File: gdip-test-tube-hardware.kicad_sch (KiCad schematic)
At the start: 52 parts, among them J1 USB_B, J2 USB_B, J3 Conn_01x06, J4 Conn_01x06, J5 Conn_01x06, J6 Screw_Terminal_01x02, Q1 BC818, Q2 BC818, Q3 BC818, SW1 SW_Push, SW2 SW_Push, U1 ESP32-S3-WROOM-1-N16R2, U2 AMS1117-3.3, U3 CP2102N-Axx-xQFN28, U4 USBLC6-2SC6, U5 USBLC6-2SC6, U6 74LVC2G00

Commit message: Removed multiplexer for buzzer and servo as we can remap any ESP32 pin. Also switched mux for shift register for the 7-seg display.
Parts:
- removed J3, J4, J5: Conn_01x06, Connector_PinHeader_2.54mm:PinHeader_1x06_P2.54mm_Vertical, symbol Connector_Generic:Conn_01x06
- added J3: Screw_Terminal_01x02, gdip-test-tube:TE_282837-2, symbol Connector:Screw_Terminal_01x02
- added R18, R19, R20, R21, R22, R23, R24, R25: 330, Resistor_SMD:R_0805_2012Metric, symbol Device:R_Small
- added SERVO_A1, SERVO_B1, SERVO_C1, SERVO_D1, SERVO_E1, SERVO_F1: Conn_01x03_Pin, Connector:FanPinHeader_1x03_P2.54mm_Vertical, symbol Connector:Conn_01x03_Pin
- added U7: HDSP-7401, Display_7Segment:HDSP-7401, symbol Display_Character:HDSP-7401
- added U8: 74AHC595, Package_SO:SOIC-16_3.9x9.9mm_P1.27mm, symbol 74xx:74AHC595
- LS1: footprint PKLCS1212E40A1-R1:SPKR_PKLCS1212E40A1-R1 -> gdip-test-tube:SPKR_PKLCS1212E40A1-R1
- U4: JLCPCB (none) -> C2687116
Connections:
- net +3.3V: now also U7.1 (CA), U7.6 (CA), U8.10 (~{SRCLR}), U8.16 (VCC)
- net +5V: now also J3.1 (Pin_1), SERVO_A1.1 (Pin_1), SERVO_B1.1 (Pin_1), SERVO_C1.1 (Pin_1), SERVO_D1.1 (Pin_1), SERVO_E1.1 (Pin_1), SERVO_F1.1 (Pin_1); no longer J6.1 (Pin_1)
- net D1+_IN: now also U4.1 (I/O1); no longer U4.3 (I/O2)
- net D1+_OUT: now also U3.4 (D+), U4.6 (I/O1); no longer U4.4 (I/O2)
- net D1-_IN: now also U4.3 (I/O2); no longer U4.1 (I/O1)
- net D1-_OUT: now also U3.5 (D-), U4.4 (I/O2); no longer U4.6 (I/O1)
- net D2+_OUT: no longer U3.4 (D+)
- net D2-_OUT: no longer U3.5 (D-)
- net GND: now also J3.2 (Pin_2), SERVO_A1.3 (Pin_3), SERVO_B1.3 (Pin_3), SERVO_C1.3 (Pin_3), SERVO_D1.3 (Pin_3), SERVO_E1.3 (Pin_3), SERVO_F1.3 (Pin_3), U8.13 (~{OE}), U8.8 (GND); no longer J6.2 (Pin_2)
- net PWM1: now also SERVO_A1.2 (Pin_2)
- net PWM2: now also SERVO_B1.2 (Pin_2)
- net PWM3: now also SERVO_C1.2 (Pin_2)
- net PWM4: now also SERVO_D1.2 (Pin_2)
- net PWM5: now also SERVO_E1.2 (Pin_2)
- net PWM6: now reaches U6.2
- net PWM6: now also U1.17 (IO9)
- net PWMX: now reaches U1.12 (IO8)
- net PWMX: now also SERVO_F1.2 (Pin_2)
- net GPIO_SR_DATA: now reaches U1.18 (IO10)
- net GPIO_SR_DATA: now also U8.14 (SER)
- net GPIO_SR_CLOCK: now reaches U1.19 (IO11)
- net GPIO_SR_CLOCK: now also U8.11 (SRCLK)
- net GPIO_SR_RCLK: now reaches U1.20 (IO12)
- net GPIO_SR_RCLK: now also U8.12 (RCLK)
- new net: R19.1, U8.1 (QB)
- new net: R19.2, U7.9 (B)
- new net: R18.1, U8.15 (QA)
- new net: R20.1, U8.2 (QC)
- new net: R21.1, U8.3 (QD)
- new net: R25.1, U8.4 (QE)
- new net: R22.1, U8.5 (QF)
- new net: R23.1, U8.6 (QG)
- new net: R24.1, U8.7 (QH)
- new net: R20.2, U7.8 (C)
- new net: R24.2, U7.7 (DP)
- new net: R23.2, U7.3 (G)
- new net: R18.2, U7.10 (A)
- new net: R25.2, U7.4 (E)
- new net: R22.2, U7.2 (F)
- new net: R21.2, U7.5 (D)
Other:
- note added: "Mounting Holes"
- note added: "SEVEN SEGMENT"
- note added: "Warning LEDs"
- note removed: "Power Pin Headers"
- moved on the sheet: C1, C2, C4, C5, C6, C8, C9, H1, H2, H3, H4, J1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

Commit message: Further work on layout.
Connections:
- net +5V: now also SERVO_A1.2 (Pin_2), SERVO_B1.2 (Pin_2), SERVO_C1.2 (Pin_2), SERVO_D1.2 (Pin_2), SERVO_E1.2 (Pin_2), SERVO_F1.2 (Pin_2); no longer SERVO_A1.1 (Pin_1), SERVO_B1.1 (Pin_1), SERVO_C1.1 (Pin_1), SERVO_D1.1 (Pin_1), SERVO_E1.1 (Pin_1), SERVO_F1.1 (Pin_1)
- net GPIO_SR_CLOCK: now also U1.20 (IO12); no longer U1.19 (IO11)
- net GPIO_SR_RCLK: now also U1.19 (IO11); no longer U1.20 (IO12)
- net PWM1: now also SERVO_D1.1 (Pin_1); no longer SERVO_A1.2 (Pin_2)
- net PWM2: now also SERVO_A1.1 (Pin_1); no longer SERVO_B1.2 (Pin_2)
- net PWM3: now also SERVO_B1.1 (Pin_1); no longer SERVO_C1.2 (Pin_2)
- net PWM4: now also SERVO_C1.1 (Pin_1); no longer SERVO_D1.2 (Pin_2)
- net PWM5: now also SERVO_E1.1 (Pin_1), U1.35 (IO42); no longer SERVO_E1.2 (Pin_2), U1.7 (IO7)
- net PWMX: now also SERVO_F1.1 (Pin_1), U1.34 (IO41); no longer SERVO_F1.2 (Pin_2), U1.12 (IO8)
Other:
- moved on the sheet: SERVO_D1, SERVO_E1, SERVO_F1

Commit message: Finished first layout added load switch for led saftey circuit,changed 47uF cap footprint. Also added extra pin headers for USB, Voltages & Gnd on board and extra GPIOs.
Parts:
- removed C1, C2: 100nF, Capacitor_SMD:C_0805_2012Metric, symbol Device:C_Small
- added C1: 1uF, Capacitor_SMD:C_0805_2012Metric, symbol Device:C
- added D2, D3: 1N5819WS, Diode_SMD:D_SOD-323, symbol Diode:1N5819WS
- added J4: Conn_01x04, Connector_PinHeader_2.54mm:PinHeader_1x04_P2.54mm_Vertical, symbol Connector_Generic:Conn_01x04
- added J5: Conn_01x03, Connector_PinHeader_2.54mm:PinHeader_1x03_P2.54mm_Vertical, symbol Connector_Generic:Conn_01x03
- added J7: Conn_01x02, Connector_PinHeader_2.54mm:PinHeader_1x02_P2.54mm_Vertical, symbol Connector_Generic:Conn_01x02
- added R26: 4.7k, Resistor_SMD:R_0805_2012Metric, symbol Device:R
- added R27: 3.9k, Resistor_SMD:R_0805_2012Metric, symbol Device:R
- added U9: TPS22810DBVT, gdip-test-tube:SOT95P280X145-6N, symbol gdip-test-tube:TPS22810DBVT
- C11: footprint Capacitor_SMD:C_0805_2012Metric -> gdip-test-tube:CAP_EEEHA1H470XP
- D1: value LED -> MCUPWR
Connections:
- net +1V5: now also R26.2, R27.1
- net +3.3V: now also J4.1 (Pin_1), R26.1
- net +5V: now also D2.1 (K), D3.1 (K), J4.2 (Pin_2); no longer C10.1, J1.1 (VBUS), J2.1 (VBUS), J3.1 (Pin_1), SERVO_A1.2 (Pin_2), SERVO_B1.2 (Pin_2), SERVO_C1.2 (Pin_2), SERVO_D1.2 (Pin_2), SERVO_E1.2 (Pin_2), SERVO_F1.2 (Pin_2), U2.3 (VI), U4.5 (VBUS), U5.5 (VBUS)
- net D1+_IN: now also U4.3 (I/O2); no longer U4.1 (I/O1)
- net D1+_OUT: now also U4.4 (I/O2); no longer U4.6 (I/O1)
- net D1-_IN: now also U4.1 (I/O1); no longer U4.3 (I/O2)
- net D1-_OUT: now also U4.6 (I/O1); no longer U4.4 (I/O2)
- net D2+_OUT: now also U1.14 (IO20), J7.2 (Pin_2)
- net D2-_OUT: now also U1.13 (IO19), J7.1 (Pin_1)
- net GND: now also J6.2 (Pin_2), C1.2, J4.4 (Pin_4), R27.2, U9.2 (GND)
- net GPIO_SR_CLOCK: now also U1.22 (IO14); no longer U1.20 (IO12)
- net GPIO_SR_RCLK: now also U1.21 (IO13); no longer U1.19 (IO11)
- net at J6.1 (Pin_1): now also C1.1, U9.6 (VOUT)
- net GPIO_EXTRA_1: now reaches U1.10 (IO17)
- net GPIO_EXTRA_1: now also J5.1 (Pin_1)
- net GPIO_EXTRA_2: now reaches U1.11 (IO18)
- net GPIO_EXTRA_2: now also J5.2 (Pin_2)
- net GPIO_EXTRA_3: now reaches U1.12 (IO8)
- net GPIO_EXTRA_3: now also J5.3 (Pin_3)
- net GPIO_LED_SWITCH: now reaches U1.29 (IO36)
- net GPIO_LED_SWITCH: now also U9.3 (EN/UVLO)
- new net: D2.2 (A), J2.1 (VBUS), U5.5 (VBUS)
- new net: D3.2 (A), J1.1 (VBUS), U4.5 (VBUS)
- new net +6V: C10.1, J3.1 (Pin_1), J4.3 (Pin_3), SERVO_A1.2 (Pin_2), SERVO_B1.2 (Pin_2), SERVO_C1.2 (Pin_2), SERVO_D1.2 (Pin_2), SERVO_E1.2 (Pin_2), SERVO_F1.2 (Pin_2), U2.3 (VI), U9.1 (VIN)
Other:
- note added: "Motor Supply (6V)"
- note added: "Power Pin Header"
- note added: "USB & Extra GPIO Pin headers"
- note removed: "Motor Supply (5V)"
- moved on the sheet: C10, C11, C12, C5, C6, C7, D1, H1, H2, H3, H4, J1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

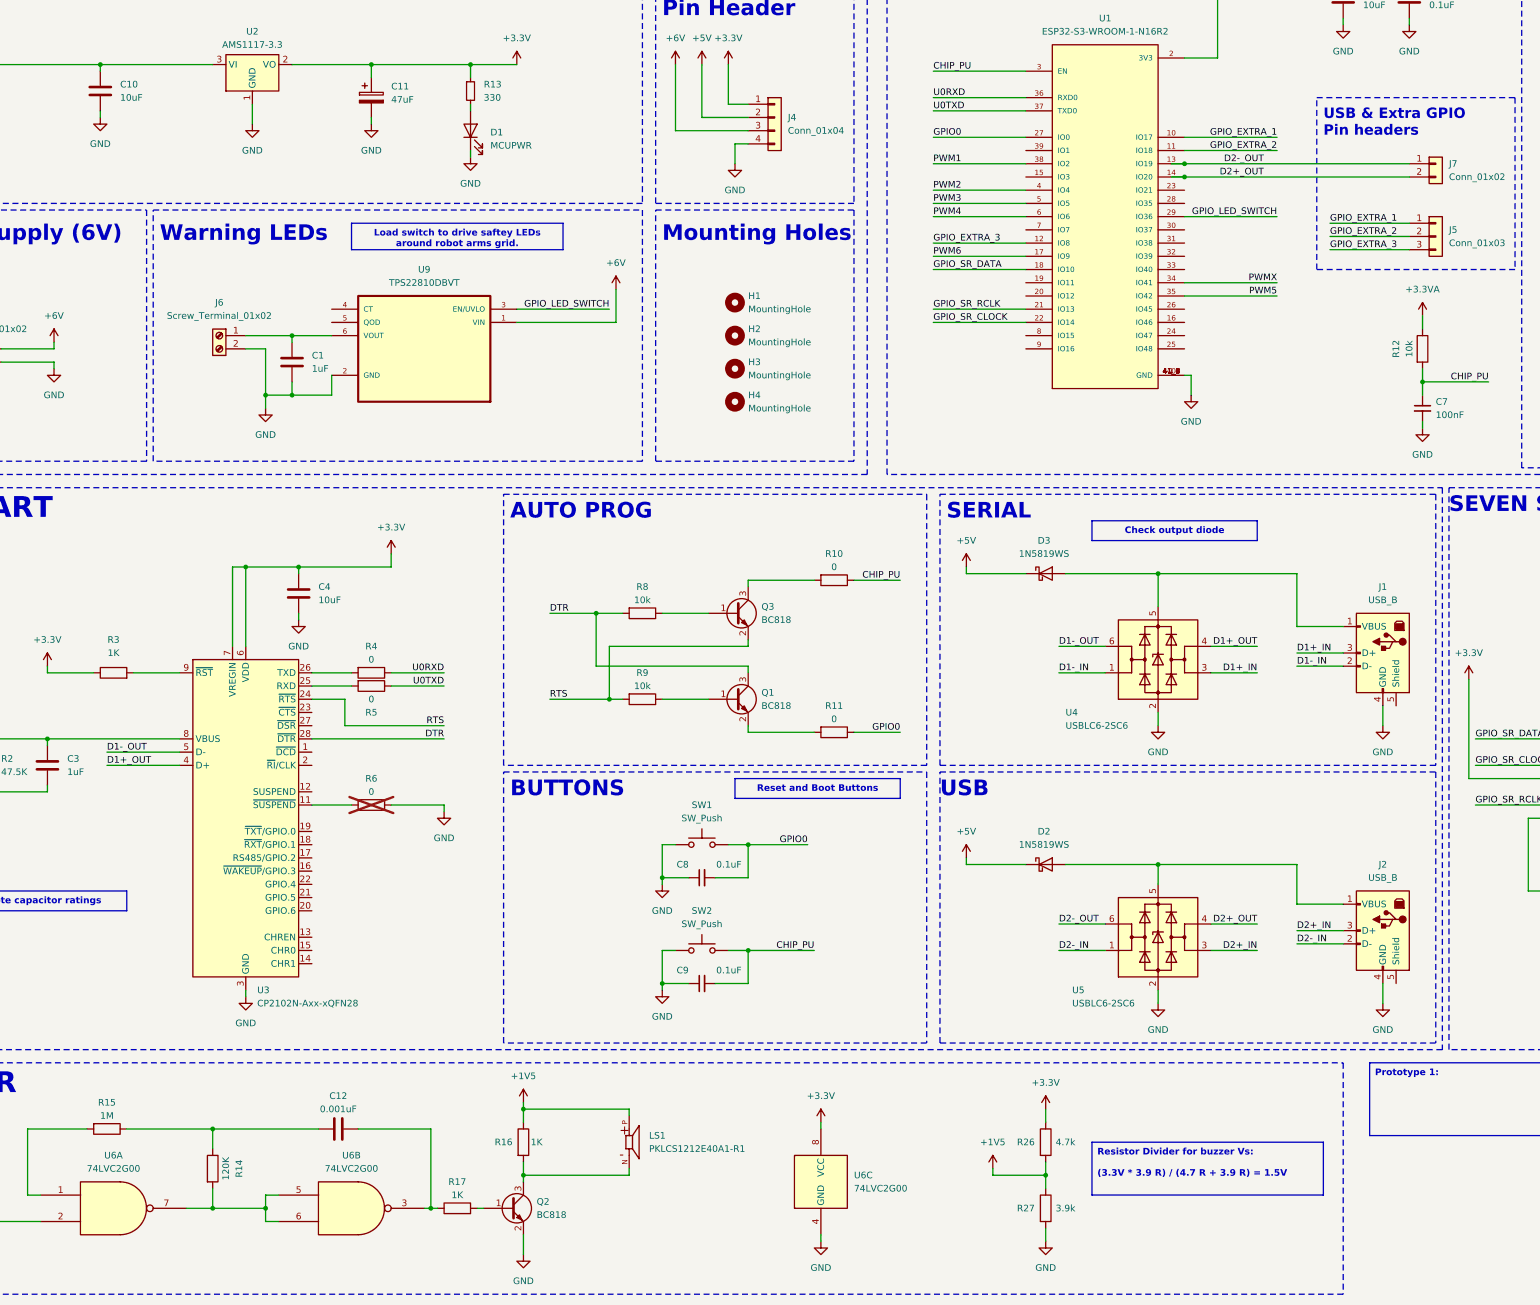
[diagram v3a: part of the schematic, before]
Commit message: Moved PWR led and added a DEBUG led in better locations. Also tested the step file of a molex part for servro headers.
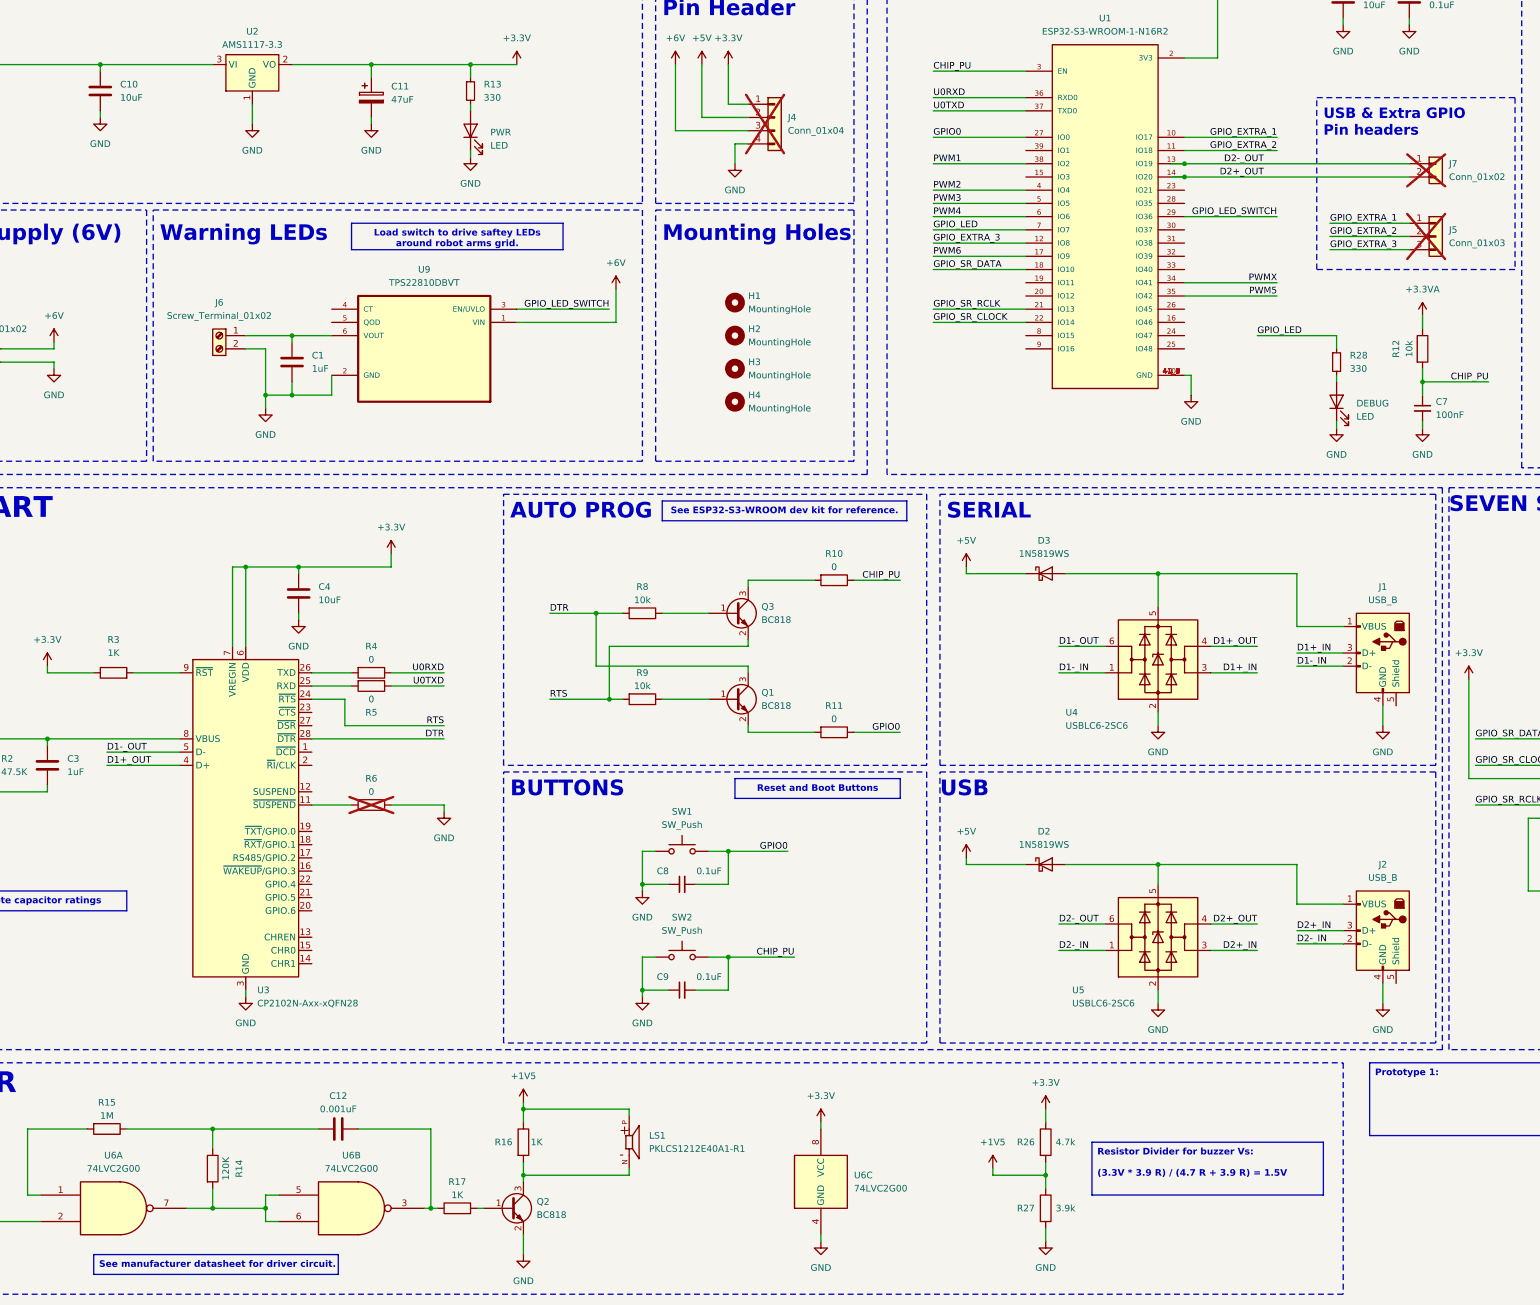
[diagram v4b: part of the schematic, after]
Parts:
- added DEBUG: LED, LED_SMD:LED_0805_2012Metric, symbol Device:LED
- added R28: 330, Resistor_SMD:R_0805_2012Metric, symbol Device:R_Small
- J4, J5, J7: now not fitted
- PWR: renamed from D1; value MCUPWR -> LED
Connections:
- net GND: now also DEBUG.1 (K)
- net GPIO_LED: now reaches U1.7 (IO7)
- net GPIO_LED: now also R28.1
- new net: DEBUG.2 (A), R28.2
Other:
- moved on the sheet: C8, C9, SW1, SW2

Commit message: Reviewed schematic and made changes please view docs folder for more info. Schematic now complete.
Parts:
- added C2: 10uF, Capacitor_SMD:C_0805_2012Metric, symbol Device:C
- C5: value 10uF -> 0.1uF
- C6: value 0.1uF -> 10uF
- C7: value 100nF -> 1uF
- renumbered DEBUG to DEBUG1, PWR to PWR1
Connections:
- net +3.3V: now also C2.1
- net +5V: no longer R1.1
- net +6V: now also C1.1
- net DTR: now also Q1.2 (E); no longer Q1.3 (C)
- net GND: now also C2.2
- net at J6.1 (Pin_1), U9.6 (VOUT): no longer C1.1
- net at R11.2: now also Q1.3 (C); no longer Q1.2 (E)
- net VBUS: now reaches D3.2 (A), J1.1 (VBUS), U4.5 (VBUS)
- net VBUS: now also R1.1
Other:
- moved on the sheet: C1
